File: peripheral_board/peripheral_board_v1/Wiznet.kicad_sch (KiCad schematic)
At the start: 22 parts, among them U4 W5500, U5 SN74AHC1G125DBVR, Y2 25MHZ

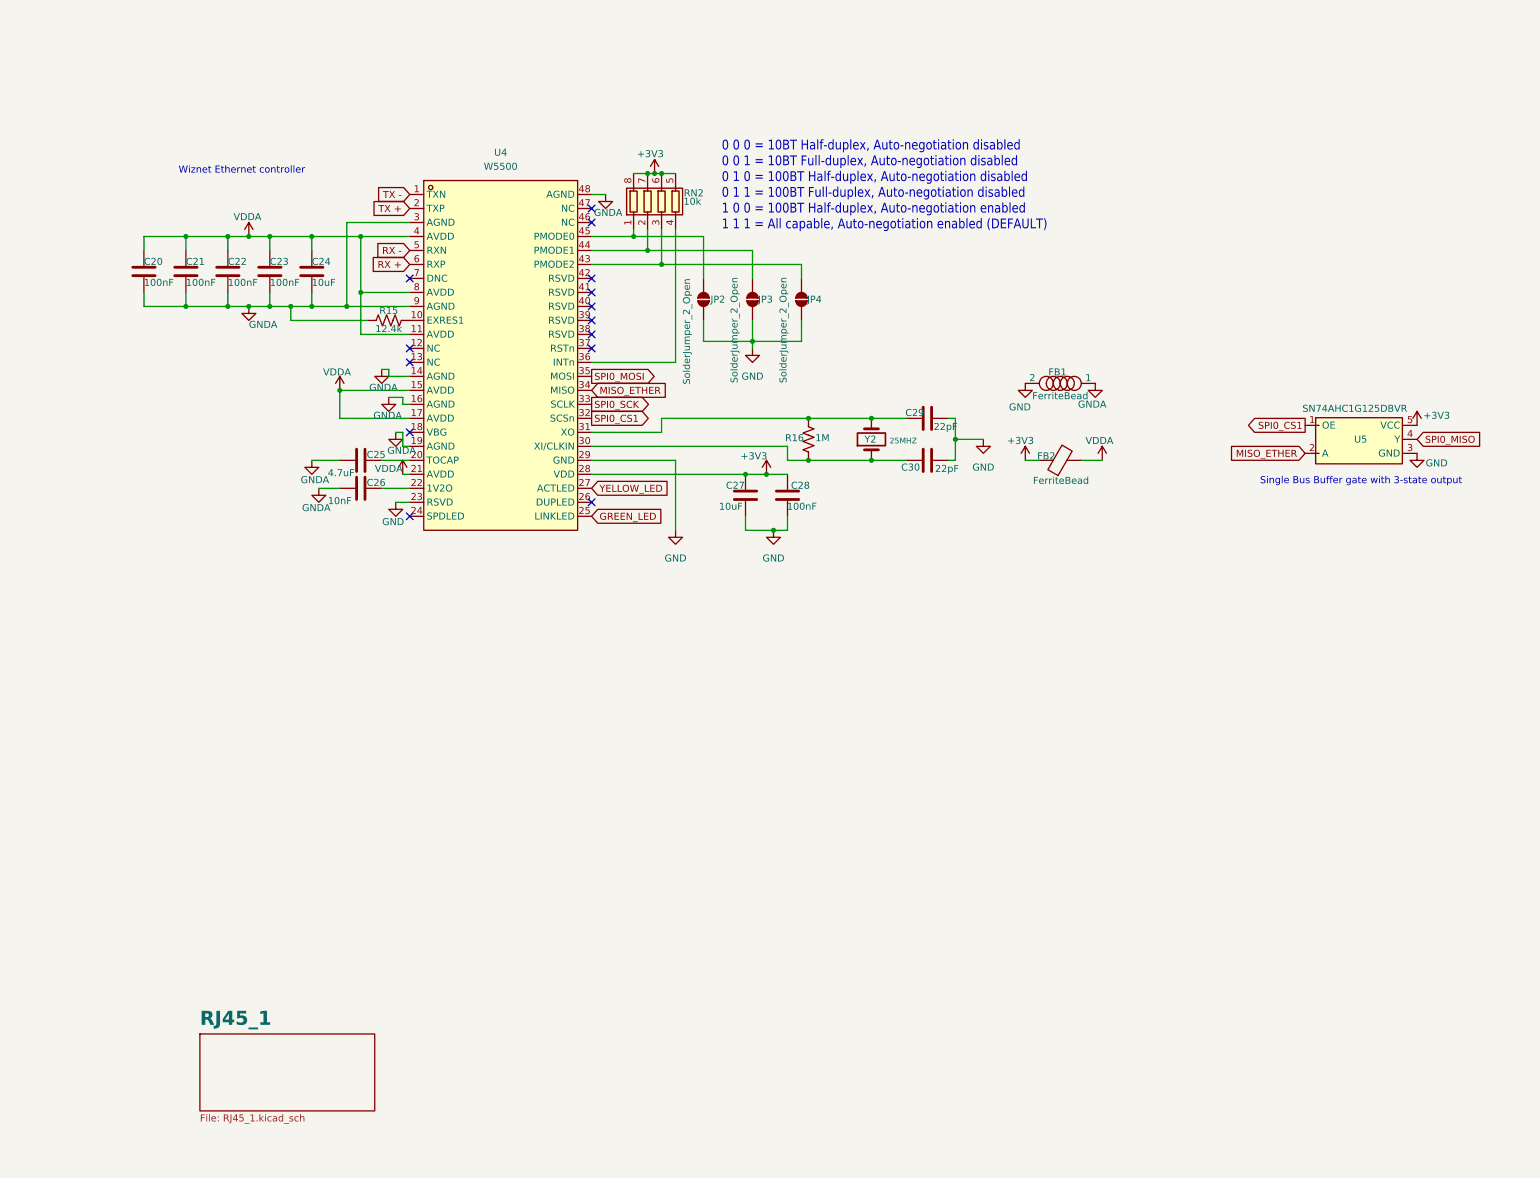
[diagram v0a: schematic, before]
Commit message: Minor KiCad Changes
Combing through my KiCad Design and making sure that everything is up to standard.
Board seems to be a bit off and doesn't seem to to be working correctly.
There are a couple things to note.

For the Wiznet there are different configurations that seem to me that were unclear and require a closer look.

For the Ethernet Switch I need to make sure it is being power correctly and I might need to had in the other ethernet switch to ensure that it works as intended because the 5th port I left open but the switch does not seem to work.
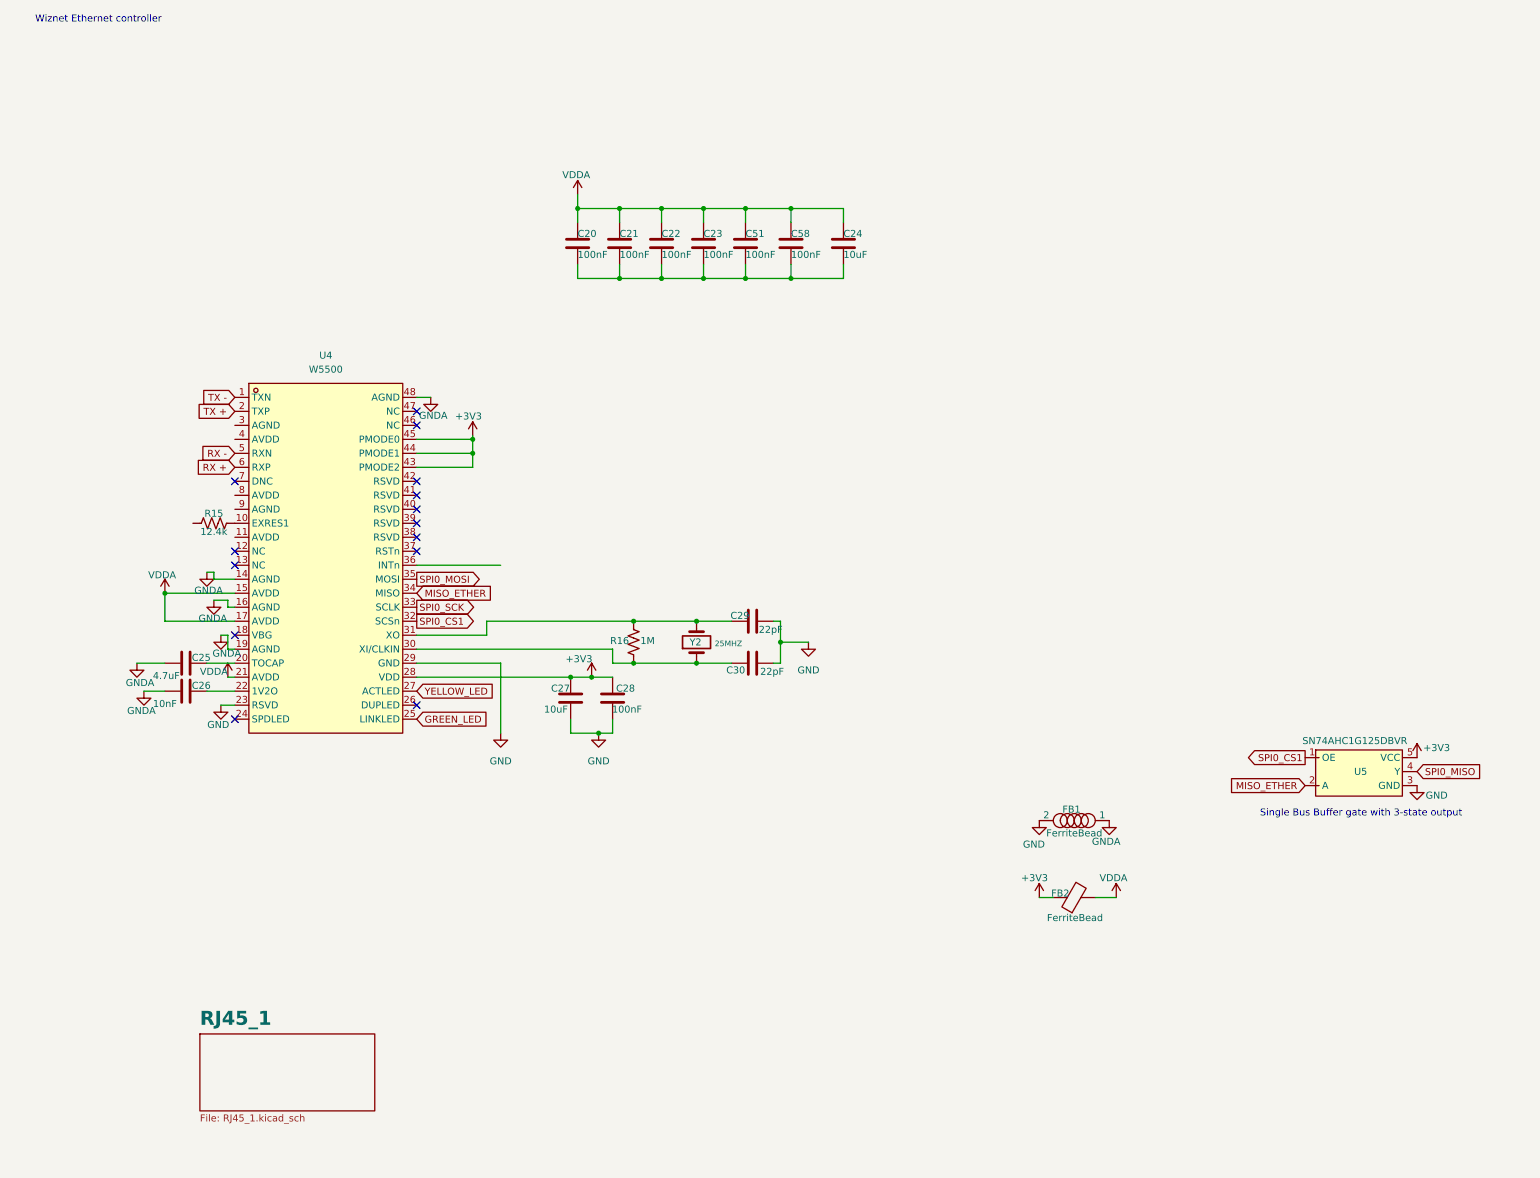
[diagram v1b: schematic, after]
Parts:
- removed JP2, JP3, JP4: SolderJumper_2_Open, Jumper:SolderJumper-2_P1.3mm_Open_RoundedPad1.0x1.5mm, symbol Jumper:SolderJumper_2_Open
- removed RN2: 10k, Resistor_SMD:R_Array_Convex_4x0603, symbol Device:R_Pack04
- added C51, C58: 100nF, Capacitor_SMD:C_0402_1005Metric, symbol Device:C
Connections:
- net +3V3: now also U4.43 (PMODE2), U4.44 (PMODE1), U4.45 (PMODE0)
- net GNDA: no longer C20.1, C21.1, C22.1, C23.1, C24.1, R15.1, U4.3 (AGND), U4.9 (AGND)
- net VDDA: now also C51.2, C58.2; no longer U4.11 (AVDD), U4.4 (AVDD), U4.8 (AVDD)
- new net: C20.1, C21.1, C22.1, C23.1, C24.1, C51.1, C58.1
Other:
- note removed: "0 0 0 = 10BT Half-duplex, Auto-negotiation disabled 0 0 1 = 10BT Full-duplex, Auto-negotiation disabled 0 1 0 = 100BT Half-duplex, Auto-negotiation disabled 0 1 1 = 100BT Full-duplex, Auto-negotiation disabled 1 0 0 = 100BT Half-duplex, Auto-negotiation enabled 1 1 1 = All capable, Auto-negotiation enabled (DEFAULT)"
- moved on the sheet: C20, C21, C22, C23, C24, C25, C26, C27, C28, C29, C30, FB1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

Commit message: Update to the board
Changed the WIZNET configuration to match that of the Pico2 eval board.
Changed the some names and some layout of the page. Not too much besides copying, reading as to why it is they way they made it and then applying.
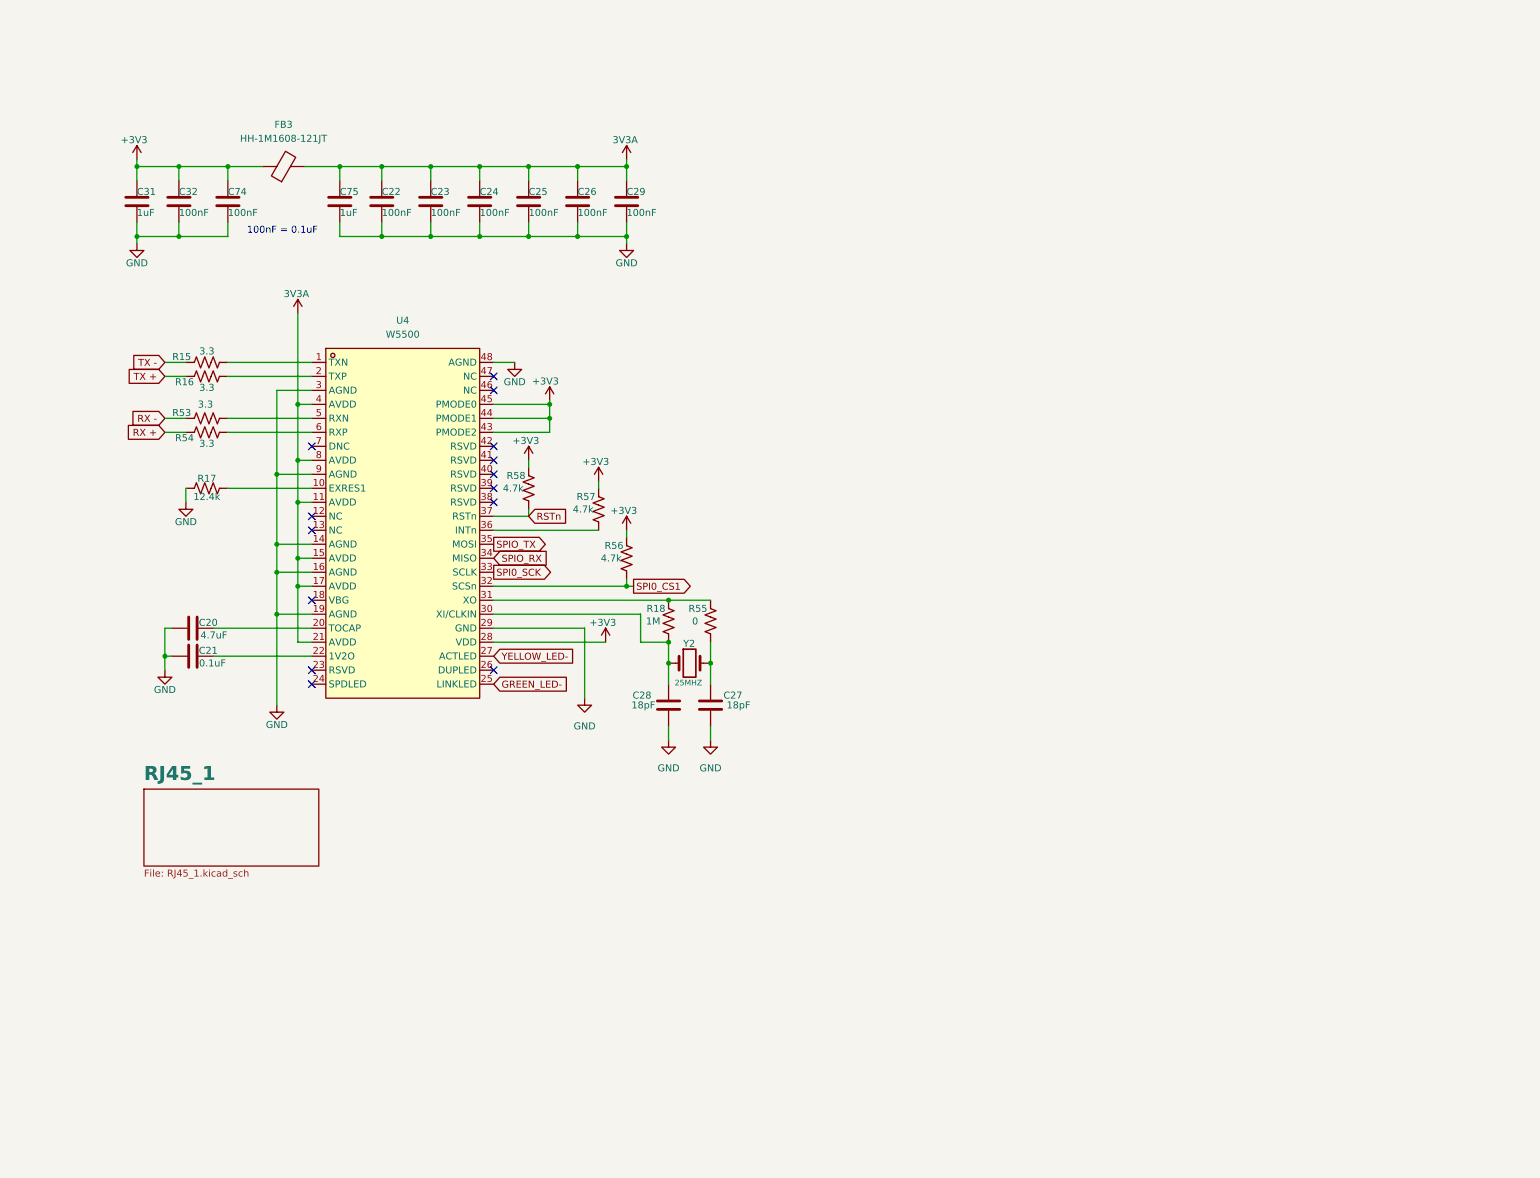
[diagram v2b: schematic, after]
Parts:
- removed C21, C22, C28, C51, C58: 100nF, Capacitor_SMD:C_0402_1005Metric, symbol Device:C
- removed C27: 10uF, Capacitor_SMD:C_0402_1005Metric, symbol Device:C
- removed FB1, FB2: FerriteBead, Inductor_SMD:L_0603_1608Metric, symbol Device:FerriteBead
- removed U5: SN74AHC1G125DBVR, easyeda2kicad:SOT-23-5_L3.0-W1.7-P0.95-LS2.8-BR, symbol easyeda2kicad:SN74AHC1G125DBVR
- added C25, C26, C29, C32, C74: 100nF, Capacitor_SMD:C_0402_1005Metric, symbol Device:C
- added C31, C75: 1uF, Capacitor_SMD:C_0402_1005Metric, symbol Device:C
- added FB3: HH-1M1608-121JT, Inductor_SMD:L_0603_1608Metric, symbol Device:FerriteBead
- added R15, R16, R53, R54: 3.3, symbol Device:R_US
- added R55: 0, Resistor_SMD:R_0603_1608Metric, symbol Device:R_US
- added R56, R57, R58: 4.7k, Resistor_SMD:R_0603_1608Metric, symbol Device:R_US
- C21: renamed from C26; value 10nF -> 0.1uF
- C24: value 10uF -> 100nF
- C27: renamed from C29; value 22pF -> 18pF
- C28: renamed from C30; value 22pF -> 18pF
- renumbered C25 to C20, C20 to C22, R15 to R17, R16 to R18
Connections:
- net GNDA is gone; now on net GND: C20.2, C21.2, U4.14 (AGND), U4.16 (AGND), U4.19 (AGND), U4.48 (AGND)
- net VDDA is gone; now on net 3V3A: C22.2, C23.2, C24.2, U4.15 (AVDD), U4.17 (AVDD), U4.21 (AVDD)
- net +3V3: now also C31.2, C32.2, C74.2, FB3.1, R56.2, R57.2, R58.2
- net GND: now also C22.1, C23.1, C24.1, R17.1, U4.3 (AGND), U4.9 (AGND), C25.1, C26.1, C29.1, C31.1, C32.1, C74.1, C75.1; no longer U4.23 (RSVD)
- net RX +: now also R54.2; no longer U4.6 (RXP)
- net RX -: now also R53.1; no longer U4.5 (RXN)
- net SPI0_CS1: now also R56.1
- net TX +: now also R16.2; no longer U4.2 (TXP)
- net TX -: now also R15.1; no longer U4.1 (TXN)
- net at C27.2, Y2.3 (2): now also R55.1; no longer R18.2, U4.31 (XO)
- net 3V3A: now reaches U4.11 (AVDD)
- net 3V3A: now also U4.4 (AVDD), U4.8 (AVDD), C25.2, C26.2, C29.2, C75.2, FB3.2
- net at U4.36 (INTn): now also R57.1
- net RSTn: now reaches U4.37 (RSTn)
- net RSTn: now also R58.1
- net GREEN_LED renamed GREEN_LED-
- net MISO_ETHER renamed SPIO_RX
- net SPI0_MOSI renamed SPIO_TX
- net YELLOW_LED renamed YELLOW_LED-
- new net: R18.2, R55.2, U4.31 (XO)
- new net: R16.1, U4.2 (TXP)
- new net: R53.2, U4.5 (RXN)
- new net: R15.2, U4.1 (TXN)
- new net: R54.1, U4.6 (RXP)
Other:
- note added: "100nF = 0.1uF"
- note removed: "Single Bus Buffer gate with 3-state output"
- note removed: "Wiznet Ethernet controller"
- moved on the sheet: C20, C21, C22, C27, C28, R17, R18, U4, Y2
